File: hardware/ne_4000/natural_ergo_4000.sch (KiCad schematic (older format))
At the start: 31 parts, among them J1 CONN_01X06, J2 CONN_02X03, J3 CONN_01X17, J4 CONN_01X17, J5 USB_OTGP, SW1 SW_Push, SW2 SW_Push, U1 ATMEGA88PA-AU, U2 74HC164, U3 74HC164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

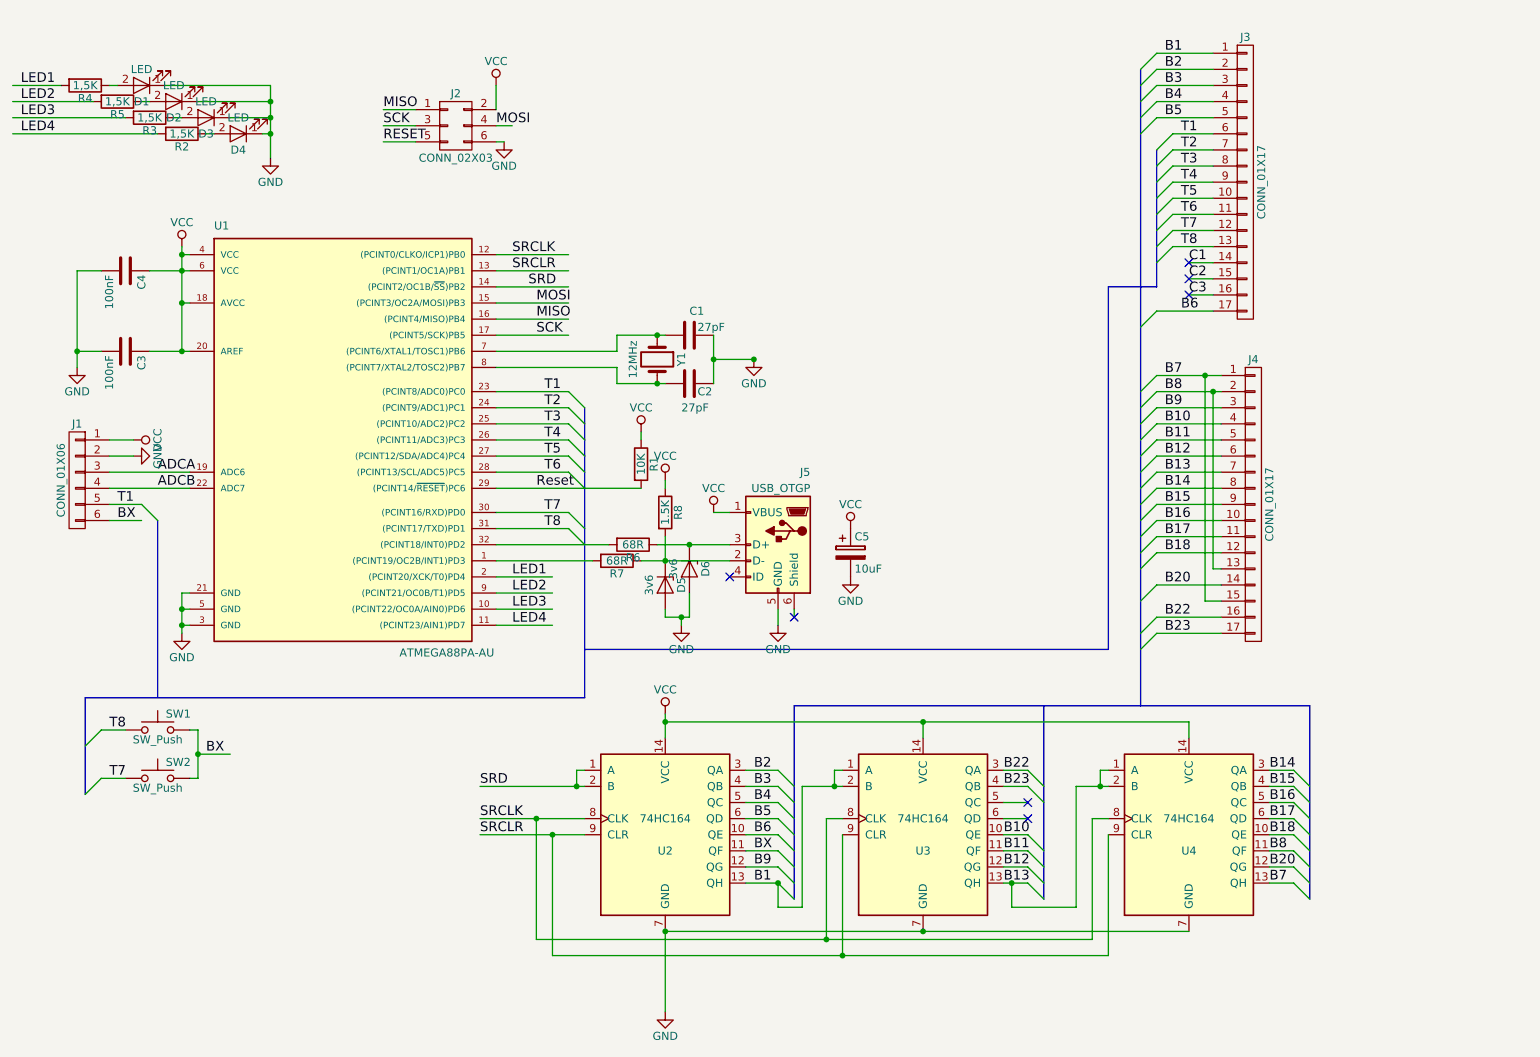
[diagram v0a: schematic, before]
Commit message: Replace shift registers with open drain version.
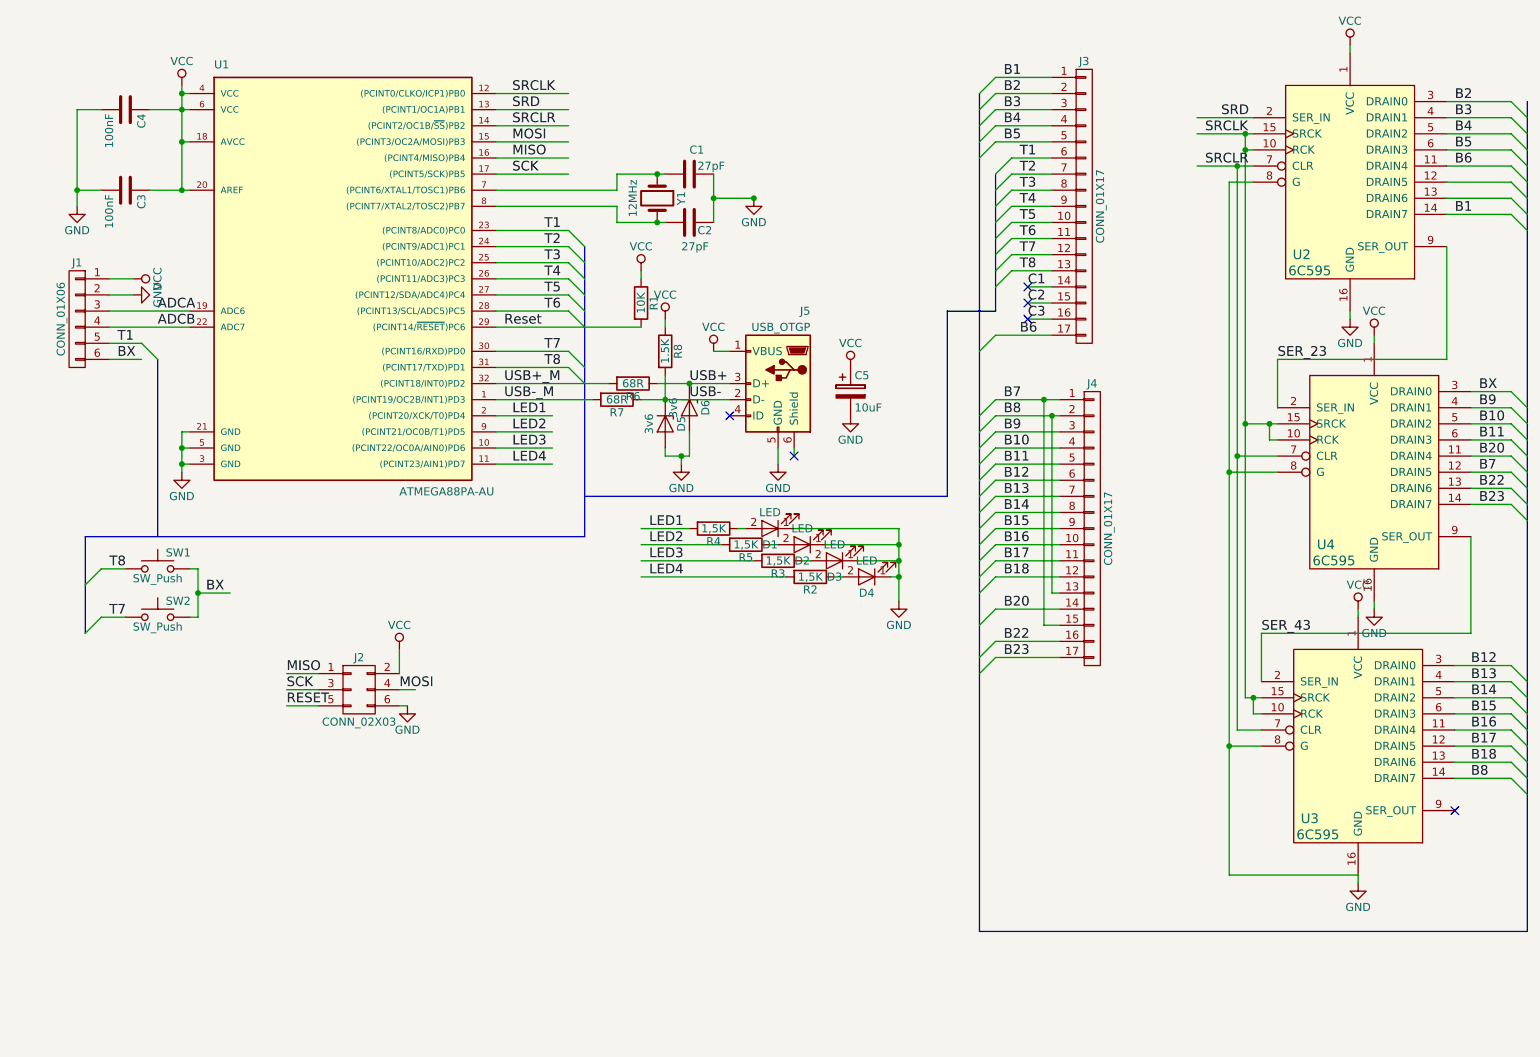
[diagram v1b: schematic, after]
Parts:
- removed U2, U3, U4: 74HC164, Housings_SOIC:SOIC-14_3.9x8.7mm_Pitch1.27mm, symbol 74HC164
- added U2, U3, U4: 6C595, Housings_SOIC:SOIC-16_3.9x9.9mm_Pitch1.27mm, symbol 6C595
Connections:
- net labels added: SER_23, SER_43, USB+, USB+_M, USB-, USB-_M
- wire segments 177 -> 175
- no-connect marks 7 -> 6
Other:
- moved on the sheet: C1, C2, C3, C4, C5, D1, D2, D3, D4, D5, D6, J1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

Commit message: Third attempt at saving kicad files.
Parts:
- C1, C2, C3, C4: symbol C -> natural_ergo_4000-rescue:C
- C5: symbol CP -> natural_ergo_4000-rescue:CP
- D1, D2, D3, D4: symbol LED -> natural_ergo_4000-rescue:LED
- D5, D6: symbol D_Zener -> natural_ergo_4000-rescue:D_Zener
- J1: symbol CONN_01X06 -> natural_ergo_4000-rescue:CONN_01X06
- J2: symbol CONN_02X03 -> natural_ergo_4000-rescue:CONN_02X03
- J3, J4: symbol CONN_01X17 -> natural_ergo_4000-rescue:CONN_01X17
- J5: symbol USB_OTGP -> natural_ergo_4000-rescue:USB_OTGP
- R1, R2, R3, R4, R5, R6, R7, R8: symbol R -> natural_ergo_4000-rescue:R
- SW1, SW2: symbol SW_Push -> natural_ergo_4000-rescue:SW_Push
- U1: symbol ATMEGA88PA-AU -> natural_ergo_4000-rescue:ATMEGA88PA-AU
- U2, U3, U4: symbol 6C595 -> natural_ergo_4000-rescue:6C595
- Y1: symbol Crystal -> natural_ergo_4000-rescue:Crystal
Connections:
- wire segments 175 -> 204
